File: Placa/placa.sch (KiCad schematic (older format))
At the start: 30 parts, among them IC1 ATMEGA328-A, P1 CONN_01X04, P12 CONN_02X03, P2 CONN_01X02, P3 CONN_01X02, P4 BallCaster2, P5 BallCaster1, P6 CONN_01X04, P7 CONN_01X04, SW1 SW_PUSH_SMALL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

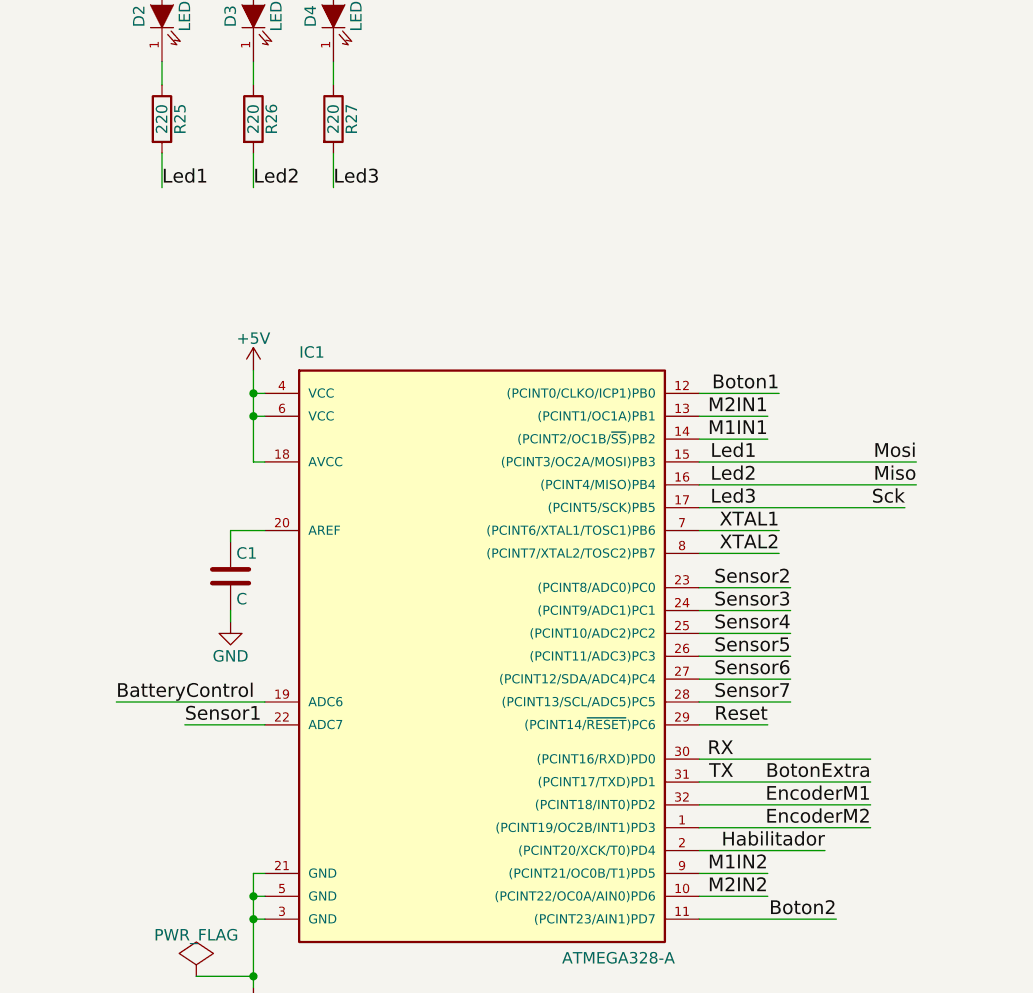
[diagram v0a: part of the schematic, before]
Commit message: Está todo ruteado, falta engrozar pistas, chequear wiki y un chequeo general
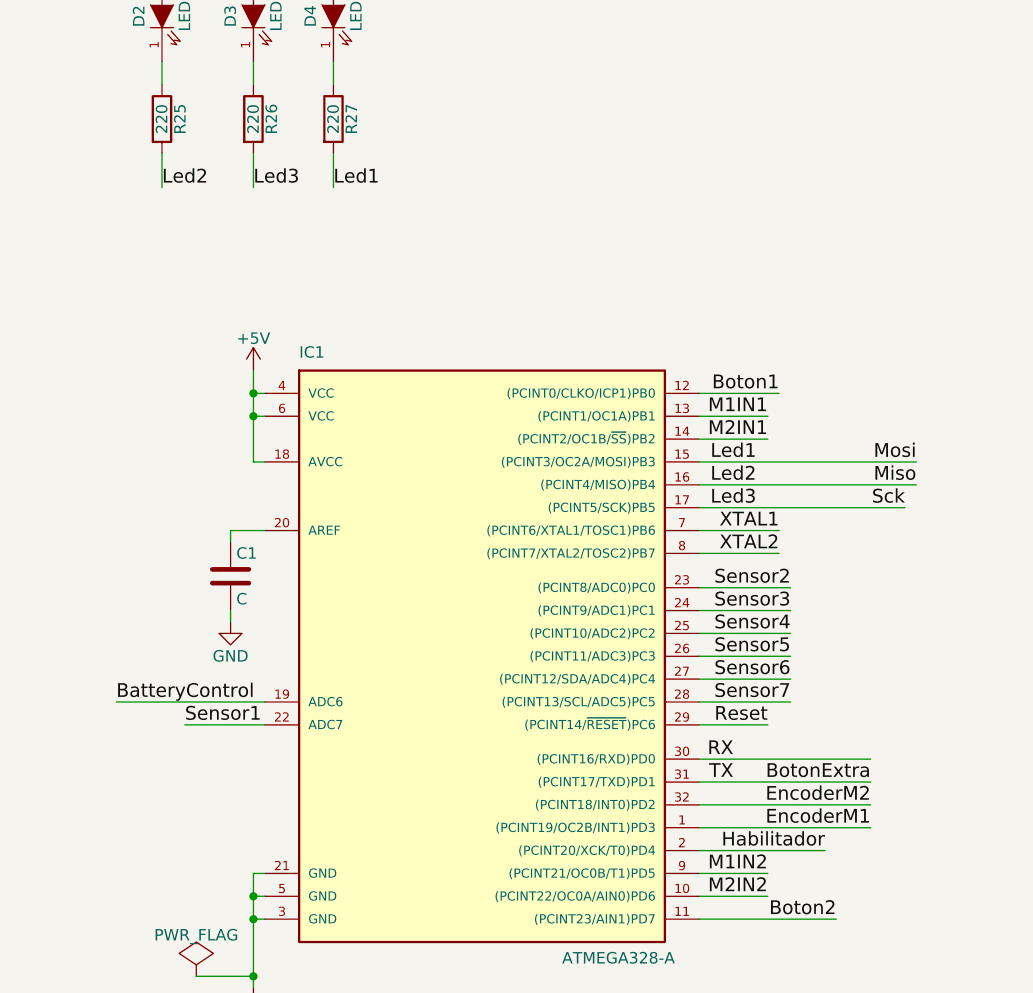
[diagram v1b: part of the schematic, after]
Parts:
- C1: footprint Capacitors_ThroughHole:C_Radial_D5_L11_P2 -> Capacitors_SMD:C_0805_HandSoldering
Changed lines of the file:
@@
 F 0 "C1" H 1725 5350 50  0000 L CNN
 F 1 "C" H 1725 5150 50  0000 L CNN
-F 2 "Capacitors_ThroughHole:C_Radial_D5_L11_P2" H 1738 5100 50  0001 C CNN
+F 2 "Capacitors_SMD:C_0805_HandSoldering" H 1738 5100 50  0001 C CNN
 F 3 "" H 1700 5250 50  0000 C CNN
 	1    1700 5250
@@
 Text Label 8550 4300 0    60   ~ 0
 M2OUT2
-Text Label 4050 4550 2    60   ~ 0
+Text Label 4050 4650 2    60   ~ 0
 M2IN1
 Text Label 4050 6650 2    60   ~ 0
@@
 Text Label 8550 3700 0    60   ~ 0
 M1OUT2
-Text Label 4050 4650 2    60   ~ 0
+Text Label 4050 4550 2    60   ~ 0
 M1IN1
 Text Label 4050 6550 2    60   ~ 0
@@
 	1    0    0    -1
 $EndComp
-Text Label 2150 3550 0    60   ~ 0
+Text Label 1800 3550 0    60   ~ 0
 Led3
 $Comp
@@
 	1    0    0    -1
 $EndComp
-Text Label 1400 3550 0    60   ~ 0
+Text Label 2150 3550 0    60   ~ 0
 Led1
 $Comp
@@
 	1    0    0    -1
 $EndComp
-Text Label 1800 3550 0    60   ~ 0
+Text Label 1400 3550 0    60   ~ 0
 Led2
 Text Label 4000 4750 2    60   ~ 0
@@
 Text Label 4100 5150 2    60   ~ 0
 XTAL2
+Text Label 4500 6250 2    60   ~ 0
+EncoderM2
 Text Label 4500 6350 2    60   ~ 0
-EncoderM2
-Text Label 4500 6250 2    60   ~ 0
 EncoderM1
 Text Label 4150 5800 2    60   ~ 0

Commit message: Agrego cambios sugeridos en la wiki de github.
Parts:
- removed P1: CONN_01X04, Pin_Headers:Pin_Header_Straight_1x04, symbol CONN_01X04
- added P1: CONN_01X05, Pin_Headers:Pin_Header_Straight_1x05, symbol CONN_01X05
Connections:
- wire segments 148 -> 149
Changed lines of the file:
@@
 LIBS:DVR8833
 LIBS:sn74lvc2g86
-LIBS:logo
-LIBS:placa-cache
 EELAYER 25 0
 EELAYER END
@@
 $EndComp
 $Comp
-L CONN_01X04 P1
-U 1 1 572D968E
-P 8250 5350
-F 0 "P1" H 8250 5600 50  0000 C CNN
-F 1 "CONN_01X04" V 8350 5350 50  0000 C CNN
-F 2 "Pin_Headers:Pin_Header_Straight_1x04" H 8250 5350 50  0001 C CNN
-F 3 "" H 8250 5350 50  0000 C CNN
-	1    8250 5350
-	1    0    0    -1
-$EndComp
-$Comp
 L +5V #PWR016
 U 1 1 572DB105
@@
 	1550 7000 1800 7000
 Connection ~ 1800 7000
+$Comp
+L CONN_01X05 P1
+U 1 1 5854844A
+P 8250 5400
+F 0 "P1" H 8250 5700 50  0000 C CNN
+F 1 "CONN_01X05" V 8350 5400 50  0000 C CNN
+F 2 "Pin_Headers:Pin_Header_Straight_1x05" H 8250 5400 50  0001 C CNN
+F 3 "" H 8250 5400 50  0000 C CNN
+	1    8250 5400
+	1    0    0    -1
+$EndComp
+Wire Wire Line
+	8050 5600 7800 5600
+Text Label 7800 5600 0    60   ~ 0
+Reset
 $EndSCHEMATC
